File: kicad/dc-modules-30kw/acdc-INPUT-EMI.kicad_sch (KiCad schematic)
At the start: 35 parts

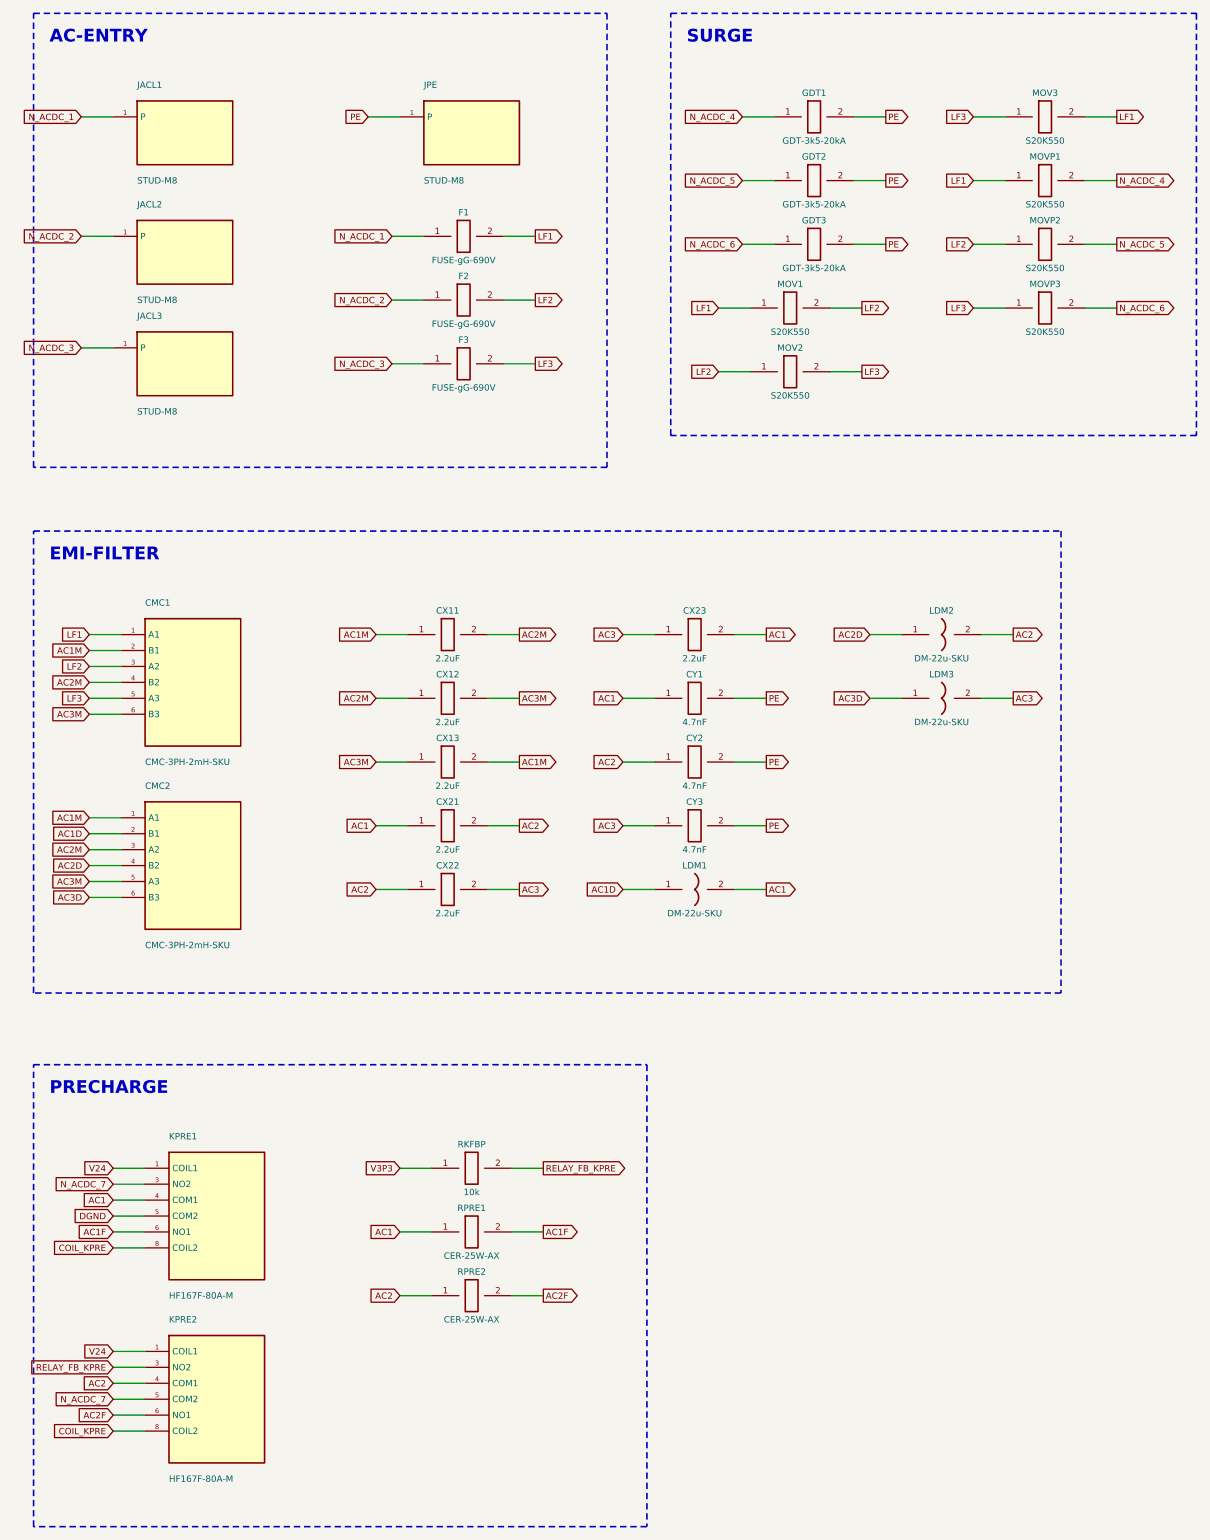
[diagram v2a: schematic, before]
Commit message: Visual pass on the hand-placed sheets: four draughting defects fixed
End-to-end inspection at zoom found four things the wide view hides:

1. The reference designator collided with the first top pin's number on
   every multi-pin IC. The library default had been moved but the INSTANCE
   property is what renders -- fixed there, right-justified clear of the body.
2. Power pins on the top/bottom edges drew their name INSIDE the body,
   rotated, straight through the first left/right pin name (VDD over PC13 on
   the MCU). Their names are now suppressed; the net label outside already
   says V3P3 / DGND, which is standard practice on a large MCU.
3. Unbound symbol pins rendered as bare stubs that read as unfinished
   connections. Every one now carries an explicit no-connect marker.
4. Single-pin parts (M8 studs, heatsink tab) were drawn by the IC path as
   large empty rectangles. They now use a real terminal symbol -- a small
   open circle on a stub -- in both the KiCad 10 and legacy generators.

Both verifiers still 100.00% (1735/1735 pins, 608 components, 0 floating
labels, 0 overlapping symbols, 0 unclosed frames). Page PDFs and the EasyEDA
import bundle regenerated against the corrected MCU pin map.

Co-Authored-By: Claude Fable 5 <noreply@anthropic.com>
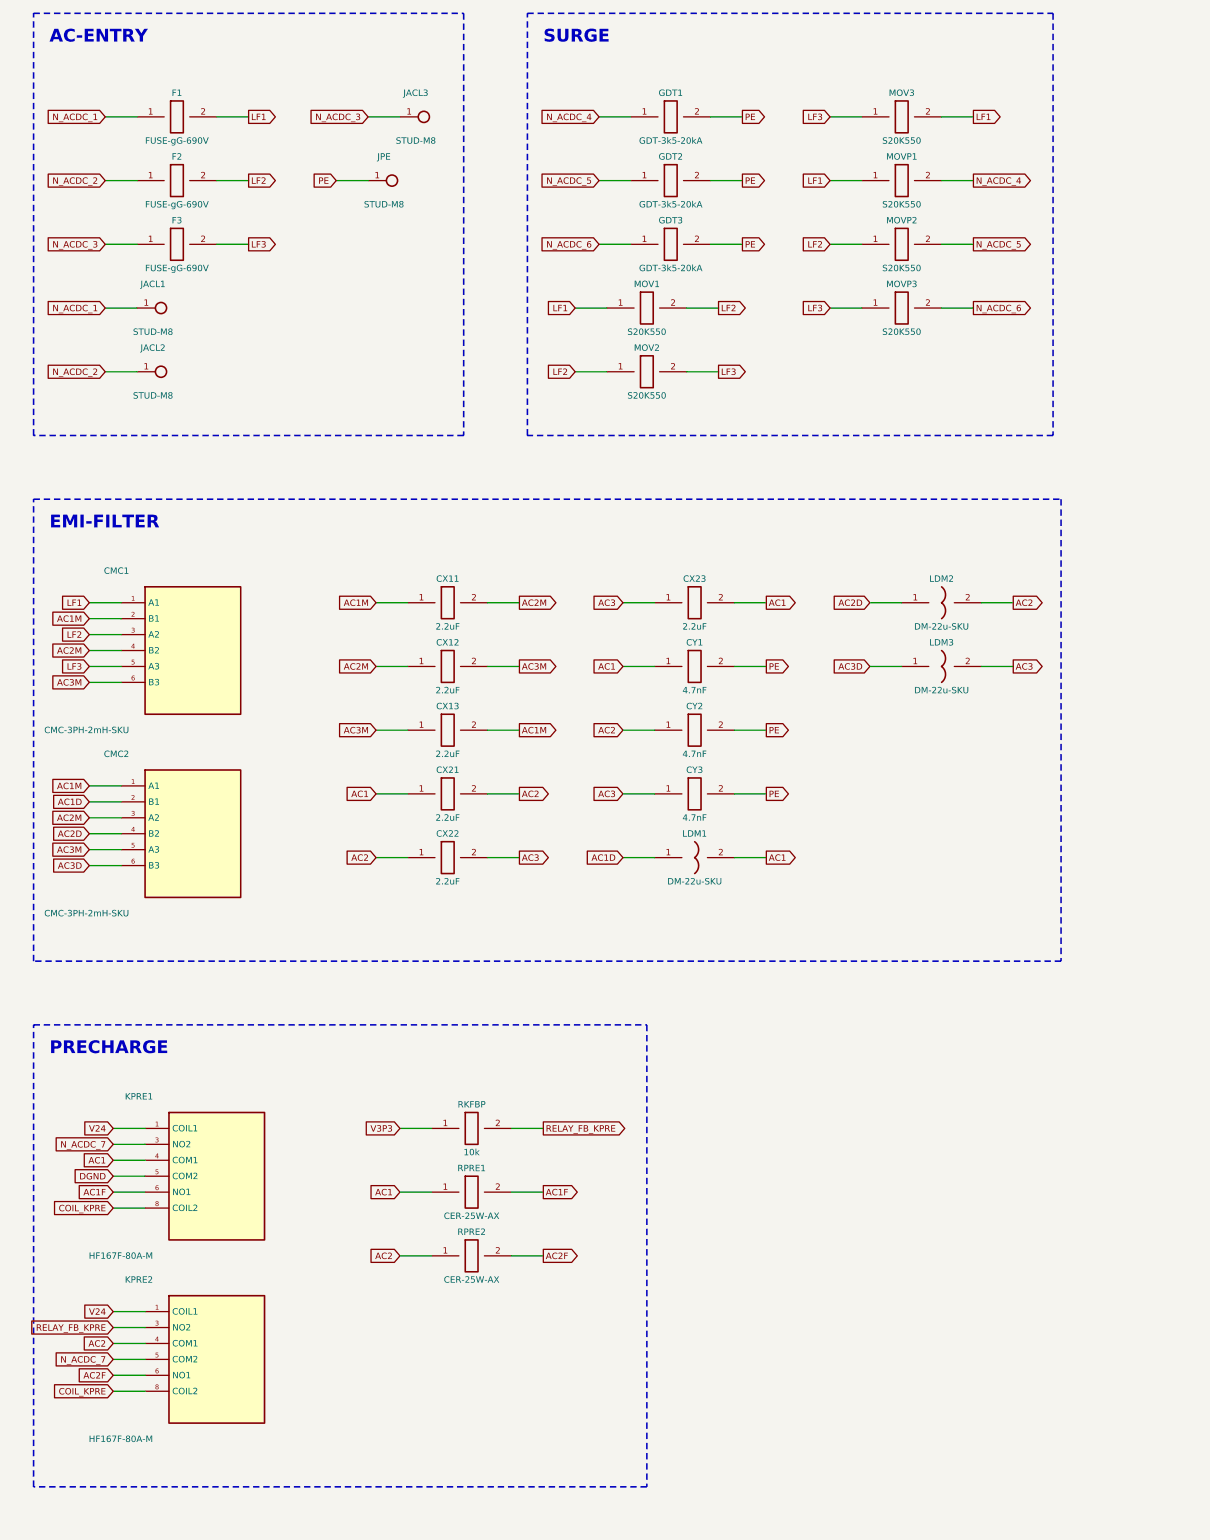
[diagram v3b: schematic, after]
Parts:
- JACL1, JACL2, JACL3, JPE: symbol dc-modules:STUD-M8 -> dc-modules:TERM_1
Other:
- moved on the sheet: CMC1, CMC2, CX11, CX12, CX13, CX21, CX22, CX23, CY1, CY2, CY3, F1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
